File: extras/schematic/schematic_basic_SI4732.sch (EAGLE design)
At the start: 18 parts, among them U2 SI4732-A10-GSR

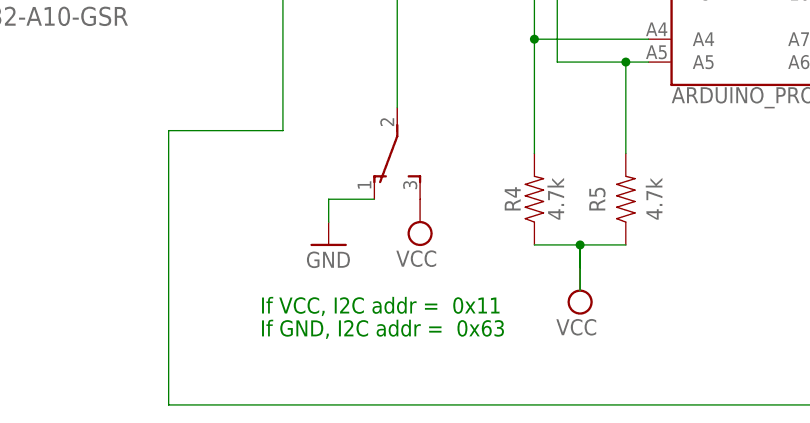
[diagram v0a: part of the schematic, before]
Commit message: SI473X Arduino Library
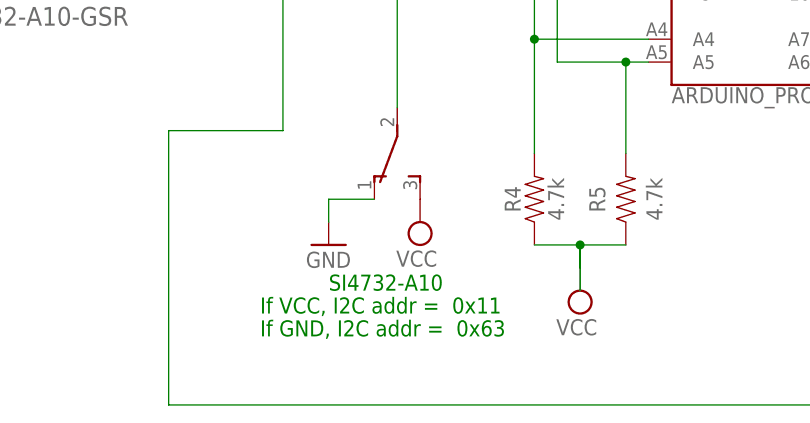
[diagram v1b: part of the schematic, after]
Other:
- note added: "SI4732-A10"
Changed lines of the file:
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@@
 <rectangle x1="-35.56" y1="137.16" x2="-20.32" y2="149.86" layer="205"/>
 <text x="-33.02" y="152.4" size="1.778" layer="205">Optional</text>
+<text x="33.02" y="58.42" size="1.778" layer="91">SI4732-A10</text>
 </plain>
 <instances>
